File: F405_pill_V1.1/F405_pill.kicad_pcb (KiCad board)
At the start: 4 copper layers, 53.8 x 19.4 mm, 42 parts, among them J1 Conn_01x04_Male, J2 Conn_01x04_Male, J4 TYPE-C-31-M-12, U1 STM32F405RGTx, U2 TCAN1051HDR, U3 LM1117-3.3, U4 STM32F405_pill, Y1 Crystal_GND24

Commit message: generated gerbers / BOMs
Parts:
- C3, C6: value 18p -> 12p
- R9: value 10k -> 20k
- U1: footprint Package_QFP:my_STM32F405RGTx_2 -> Package_QFP:LQFP-64_10x10mm_P0.5mm
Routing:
- net PC3: track 22.2 -> 0.00 mm, vias 1 -> 0
- net PC9: track 10.6 -> 32.8 mm, vias 0 -> 1
- net PA9: track 10.6 -> 29.6 mm, vias 1 -> 2
- net PC13: track 18.9 -> 0.00 mm, vias 2 -> 0
- net PA15: track 0.00 -> 18.9 mm, vias 0 -> 2
- net PC14: track 18.6 -> 0.00 mm, vias 2 -> 0
- net PC10: track 0.00 -> 18.6 mm, vias 0 -> 2
- net PA8: track 9.60 -> 28.1 mm, vias 1 -> 2
- net PC0: track 17.6 -> 0.00 mm, vias 1 -> 0
- net PC1: track 17.2 -> 0.00 mm, vias 1 -> 0
- net PC2: track 15.8 -> 0.00 mm, vias 1 -> 0
- net PC8: track 46.4 -> 61.9 mm, vias 1 -> 2
- net PB3: track 15.5 -> 0.00 mm, vias 1 -> 0
- net PC15: track 14.3 -> 0.00 mm, vias 2 -> 0
- net PC11: track 0.00 -> 14.3 mm, vias 0 -> 2
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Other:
- board text added: "STM32F405RG PILL V1.1"
- board text removed: "STM32F405RG PILL V1.0"

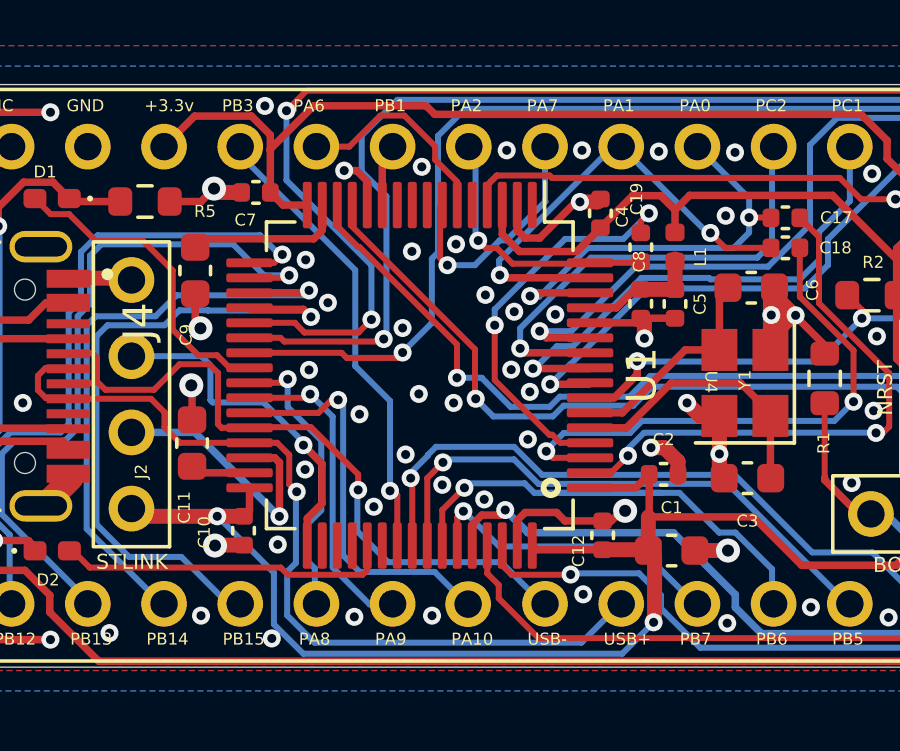
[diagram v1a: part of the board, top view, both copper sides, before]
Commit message: fixed orientation of U1 :-(
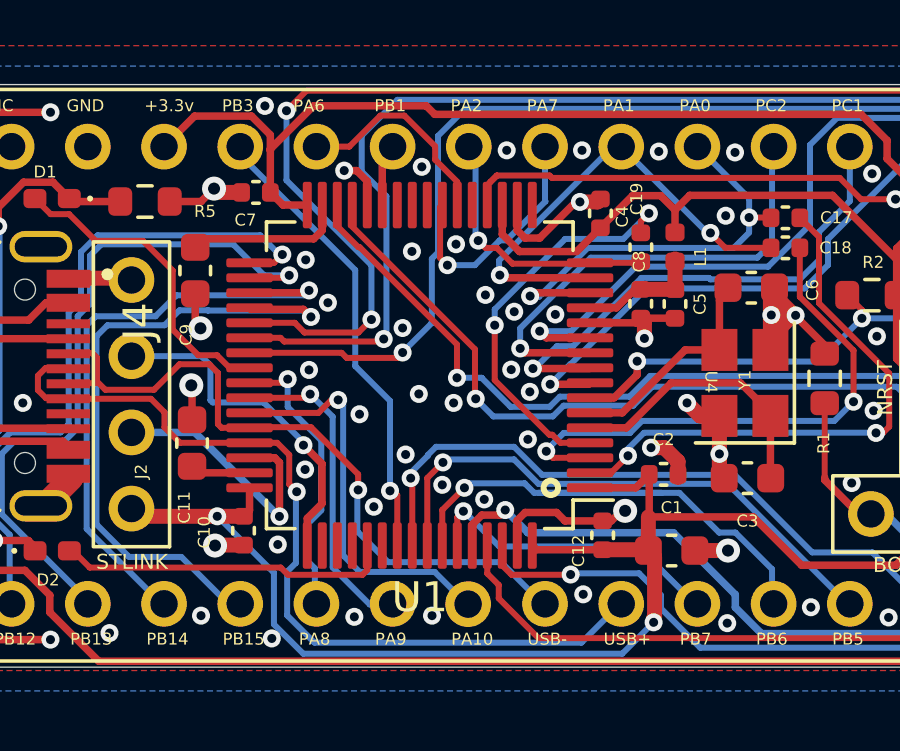
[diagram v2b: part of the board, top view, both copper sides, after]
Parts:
- turned U1 to 180 degrees
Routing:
- net PC3: track 0.00 -> 22.2 mm, vias 0 -> 1
- net PC9: track 32.8 -> 10.6 mm, vias 1 -> 0
- net PA9: track 29.6 -> 10.6 mm, vias 2 -> 1
- net PC13: track 0.00 -> 18.9 mm, vias 0 -> 2
- net PA15: track 18.9 -> 0.00 mm, vias 2 -> 0
- net PC14: track 0.00 -> 18.6 mm, vias 0 -> 2
- net PC10: track 18.6 -> 0.00 mm, vias 2 -> 0
- net PA8: track 28.1 -> 9.60 mm, vias 2 -> 1
- net PC0: track 0.00 -> 17.6 mm, vias 0 -> 1
- net PC1: track 0.00 -> 17.2 mm, vias 0 -> 1
- net PC2: track 0.00 -> 15.8 mm, vias 0 -> 1
- net PC8: track 61.9 -> 46.4 mm, vias 2 -> 1
- net PB3: track 0.00 -> 15.5 mm, vias 0 -> 1
- net PC15: track 0.00 -> 14.3 mm, vias 0 -> 2
- net PC11: track 14.3 -> 0.00 mm, vias 2 -> 0
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
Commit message: new work
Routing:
- net GND: track 70.4 -> 67.0 mm
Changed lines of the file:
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@@
   (segment (start 122.48 86.033) (end 121.833 86.033) (width 0.5) (layer "F.Cu") (net 2))
   (segment (start 105.007 82.937) (end 105.182 83.112) (width 0.25) (layer "F.Cu") (net 2))
-  (segment (start 137.016628 80.687008) (end 137.016628 80.270657) (width 0.25) (layer "F.Cu") (net 2))
   (segment (start 125.02 82.73) (end 124.87 82.73) (width 0.5) (layer "F.Cu") (net 2))
   (segment (start 124.18 82.021) (end 124.443 81.758) (width 0.5) (layer "F.Cu") (net 2))
@@
   (segment (start 131.782 79.087) (end 132.387 79.087) (width 0.25) (layer "F.Cu") (net 2))
   (segment (start 117.831068 78.9) (end 118.417 78.9) (width 0.5) (layer "F.Cu") (net 2))
-  (segment (start 139.140277 82.810657) (end 137.016628 80.687008) (width 0.25) (layer "F.Cu") (net 2))
   (segment (start 124.316 82.026) (end 125.02 82.73) (width 0.5) (layer "F.Cu") (net 2))
   (segment (start 139.517028 82.810657) (end 139.140277 82.810657) (width 0.25) (layer "F.Cu") (net 2))

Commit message: new notes
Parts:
- added C21: ??, Capacitor_SMD:C_0402_1005Metric, F.Cu at (95.4, 96.5)
- added R12: 1k, Resistor_SMD:R_0402_1005Metric, F.Cu at (125.0, 90.0)
- added R6: ??, Resistor_SMD:R_0402_1005Metric, F.Cu at (99.3, 96.3)
- added R7: 20k, Resistor_SMD:R_0402_1005Metric, F.Cu at (100.9, 79.0)
- added R8: 1k, Resistor_SMD:R_0402_1005Metric, F.Cu at (123.9, 89.9)
- D3: footprint LED_SMD:LED_0603_1608Metric -> LED_SMD:LED_0402_1005Metric_Pad0.77x0.64mm_HandSolder
- R1, R10, R11, R2, R3, R4, R9: footprint Resistor_SMD:R_0603_1608Metric -> Resistor_SMD:R_0402_1005Metric
- R5: value 5k -> 20k; footprint Resistor_SMD:R_0603_1608Metric -> Resistor_SMD:R_0402_1005Metric
- moved R11 14.0 mm to (97.0, 78.3), turned to 90 degrees
- moved R5 11.8 mm to (101.5, 90.5), turned to 0 degrees
- moved D2 5.53 mm to (105.8, 90.6)
- moved R1 3.24 mm to (127.8, 87.5), turned to 180 degrees
- moved D1 2.91 mm to (103.1, 79.0), turned to 0 degrees
- moved R9 2.07 mm to (132.1, 82.0), turned to 90 degrees
- moved R2 1.70 mm to (129.3, 82.0), turned to 0 degrees
- moved R3 1.38 mm to (142.6, 80.9)
- moved R10 1.11 mm to (97.0, 76.2)
- moved C12 1.04 mm to (117.7, 90.5), turned to 0 degrees
- moved D3 0.86 mm to (130.9, 81.9), turned to -90 degrees
- moved C10 0.76 mm to (106.0, 89.4), turned to 180 degrees
- moved C1 0.72 mm to (120.2, 90.2)
- moved JP1 0.50 mm to (129.1, 88.9)
- moved C7 0.27 mm to (107.2, 78.8)
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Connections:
- D2 pad 1: Net-(D1-Pad1) -> Net-(D2-Pad1)
- R5 pad 2: Net-(D1-Pad1) -> Net-(D2-Pad1)
- U1 pad 24: PC4 -> DUAL1
- U1 pad 25: PC5 -> DUAL2
- U2 pad 5: GND -> unconnected-(U2-Pad5)
- U4 pad 17: PB3 -> PA5
- U4 pad 28: USB_D- -> DUAL1
- U4 pad 29: USB_D+ -> DUAL2
- U4 pad 30: PB7 -> PB3
- U4 pad 31: PB6 -> PB4
- U4 pad 33: PB4 -> PB6
- U4 pad 34: PB10 -> PB7
- U4 pad 35: PB11 -> PC10
- U4 pad 36: PB8 -> PC11
- U4 pad 37: PB9 -> PC12
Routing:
- net +3V3: track 132.5 -> 70.5 mm
- net PB9: track 45.7 -> 0.00 mm, vias 2 -> 0
- net PB8: track 35.3 -> 0.00 mm, vias 1 -> 0
- net Net-(JP1-Pad2): track 28.8 -> 2.00 mm
- net PB11: track 33.9 -> 7.44 mm, vias 1 -> 0
- net PB10: track 32.4 -> 8.16 mm, vias 1 -> 0
- net USB_D+: track 28.8 -> 9.72 mm, vias 1 -> 0
- net DUAL1: track 0.00 -> 18.9 mm
- net DUAL2: track 0.00 -> 17.6 mm
- net Net-(D1-Pad1): track 17.7 -> 1.17 mm, vias 2 -> 0
- net PB4: track 22.1 -> 7.20 mm
- net USB_D-: track 23.6 -> 10.3 mm, vias 1 -> 0
- net PB7: track 10.3 -> 21.4 mm
- net PA5: track 0.00 -> 10.4 mm
- net PB3: track 15.5 -> 5.81 mm
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
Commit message: new text
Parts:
- C1: footprint Capacitor_SMD:C_0603_1608Metric -> Capacitor_SMD:C_0402_1005Metric
- moved JP2 4.05 mm to (127.1, 82.4)
- moved D3 2.47 mm to (132.1, 79.8), turned to 90 degrees
- moved JP1 2.19 mm to (127.1, 88.0), turned to 90 degrees
- moved C18 1.85 mm to (123.2, 79.3)
- moved C17 1.74 mm to (123.2, 80.3)
- moved C1 1.60 mm to (118.8, 89.4)
- moved R1 1.00 mm to (128.8, 87.3), turned to 90 degrees
- moved R2 0.71 mm to (128.7, 81.6), turned to 90 degrees
- moved C7 0.15 mm to (107.3, 78.9)
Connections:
- D2 pad 2: PC12 -> PA15
- U4 pad 35: PC10 -> PC12
- U4 pad 37: PC12 -> PC10
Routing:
- net +3V3: track 70.5 -> 30.9 mm, vias 6 -> 3
- net PC10: track 0.00 -> 33.9 mm
- net PC11: track 0.00 -> 30.1 mm
- net PB9: track 0.00 -> 27.6 mm, vias 0 -> 2
- net PB8: track 0.00 -> 24.8 mm, vias 0 -> 2
- net PC12: track 5.59 -> 27.0 mm
- net PB11: track 7.44 -> 24.5 mm, vias 0 -> 2
- net Net-(JP1-Pad2): track 2.00 -> 17.1 mm
- net PB10: track 8.16 -> 21.1 mm, vias 0 -> 2
- net DUAL2: track 17.6 -> 27.9 mm, vias 0 -> 1
- net PB4: track 7.20 -> 15.7 mm
- net DUAL1: track 18.9 -> 27.1 mm, vias 0 -> 1
- net GND: track 70.8 -> 63.1 mm, vias 70 -> 54
- net PB3: track 5.81 -> 13.0 mm
- net PC13: track 18.9 -> 13.9 mm
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
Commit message: new high amp pic
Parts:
- added C22: C_Polarized_Small, Capacitor_SMD:C_0603_1608Metric, F.Cu at (136.1, 80.7)
- added C23: C_Polarized_Small, Capacitor_SMD:C_0603_1608Metric, F.Cu at (129.3, 81.1)
- added U5: HT7550-1, Package_TO_SOT_SMD:SOT-89-3, F.Cu at (132.7, 81.2)
- C21: value ?? -> 10n
- R6: value ?? -> 47 ohm
- U2: value TCAN1051HDR -> MAX3051EKA+T; footprint Package_SO:SOIC-8_3.9x4.9mm_P1.27mm -> Package_TO_SOT_SMD:SOT-23-8
- moved R9 6.60 mm to (130.9, 88.5)
- moved D3 6.60 mm to (130.9, 86.3)
- moved C21 5.76 mm to (96.9, 90.9), turned to 90 degrees
- moved R6 4.17 mm to (96.9, 92.9), turned to -90 degrees
- moved R2 3.01 mm to (126.6, 79.4), turned to 0 degrees
- moved U2 1.90 mm to (138.9, 81.0)
- moved C2 0.52 mm to (120.2, 88.3)
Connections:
- C21 pad 1: unconnected-(C21-Pad1) -> PB12
- C21 pad 2: unconnected-(C21-Pad2) -> GND
- R6 pad 1: unconnected-(R6-Pad1) -> PB12
- R6 pad 2: unconnected-(R6-Pad2) -> _PB12
- U2 pad 3: +5V -> VDO_I
- U4 pad 21: PB12 -> _PB12
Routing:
- net GND: track 63.1 -> 71.0 mm, vias 54 -> 68
- net +5V: track 94.3 -> 102.0 mm
- net VDO_I: track 0.00 -> 4.49 mm
- net PB8: track 24.8 -> 28.8 mm
- net +3V3: track 30.9 -> 33.4 mm, vias 3 -> 10
- net _PB12: track 0.00 -> 2.40 mm
- net PB9: track 27.6 -> 29.5 mm
- net PB12: track 18.9 -> 20.0 mm, vias 1 -> 2
- net PC10: track 33.9 -> 33.2 mm
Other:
- board text added: "DUAL1"
- board text added: "DUAL2"
- board text added: "PA5"
- board text added: "PC10"
- board text added: "PC11"
- board text added: "PC12"
- board text removed: "PB10"
- board text removed: "PB11"
- board text removed: "PB8"
- board text removed: "PB9"
- board text removed: "TERM RES1"
- board text removed: "TERM RES2"
- board text removed: "USB+"
- board text removed: "USB-"

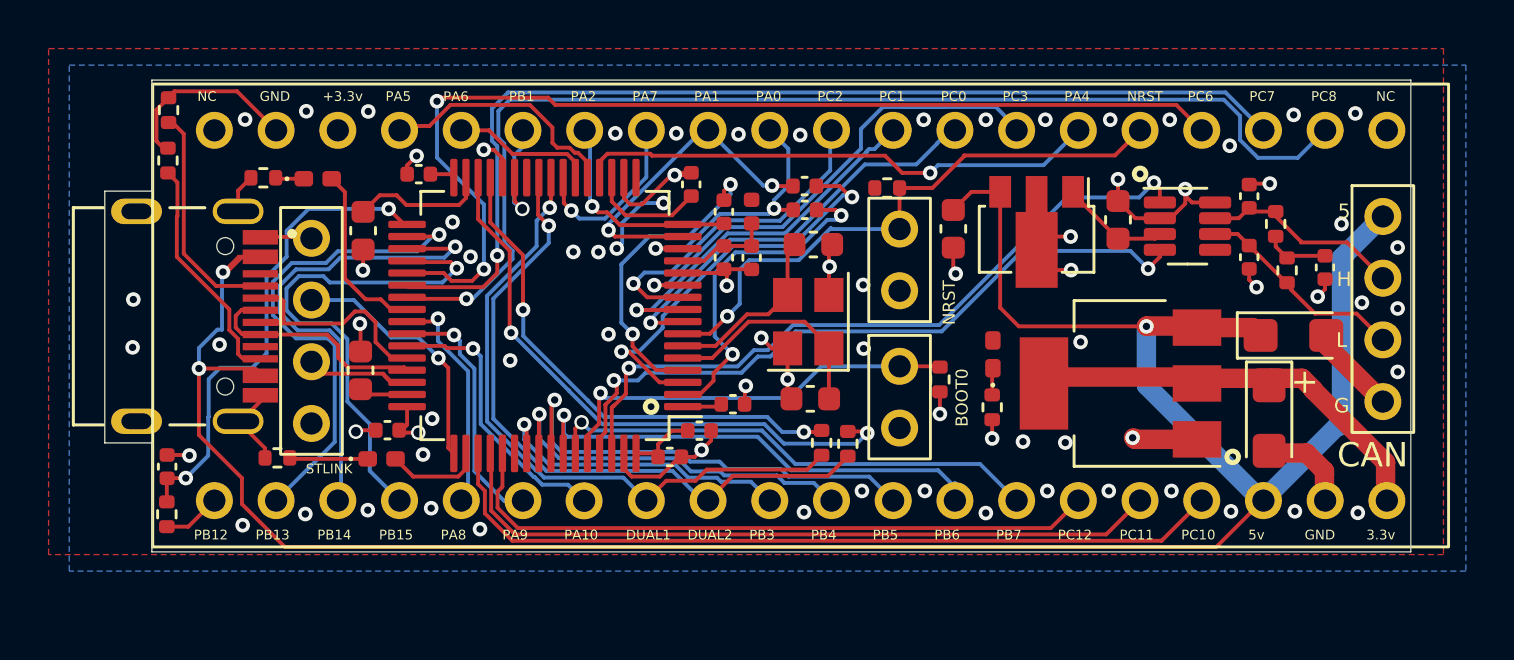
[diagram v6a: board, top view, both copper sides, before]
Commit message: added a lot of LCSC#s
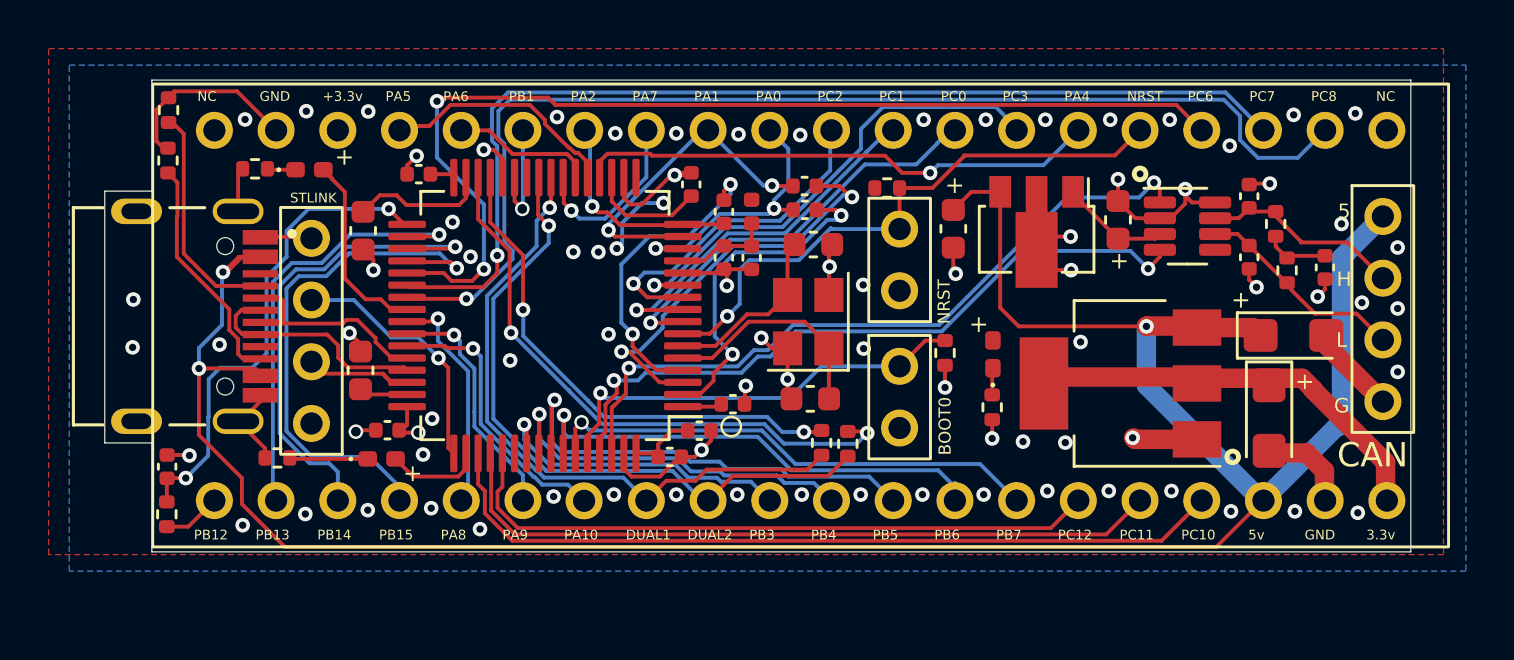
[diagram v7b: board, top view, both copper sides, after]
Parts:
- moved R1 1.11 mm to (129.0, 86.2)
- moved R7 0.50 mm to (100.6, 78.6)
- moved D1 0.50 mm to (102.8, 78.7)
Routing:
- net PB13: track 20.8 -> 18.1 mm
- net PB15: track 21.2 -> 22.1 mm
- net USB_D-: track 10.3 -> 9.59 mm
- net Net-(JP1-Pad2): track 17.3 -> 17.9 mm
- net PC9: track 7.42 -> 7.93 mm
- net GND: track 71.0 -> 71.1 mm, vias 68 -> 73

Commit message: finalizing
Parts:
- D3: value RED_LED -> RED
- moved J4 2.52 mm to (98.2, 84.7)
